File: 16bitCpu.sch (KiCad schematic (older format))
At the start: 0 parts

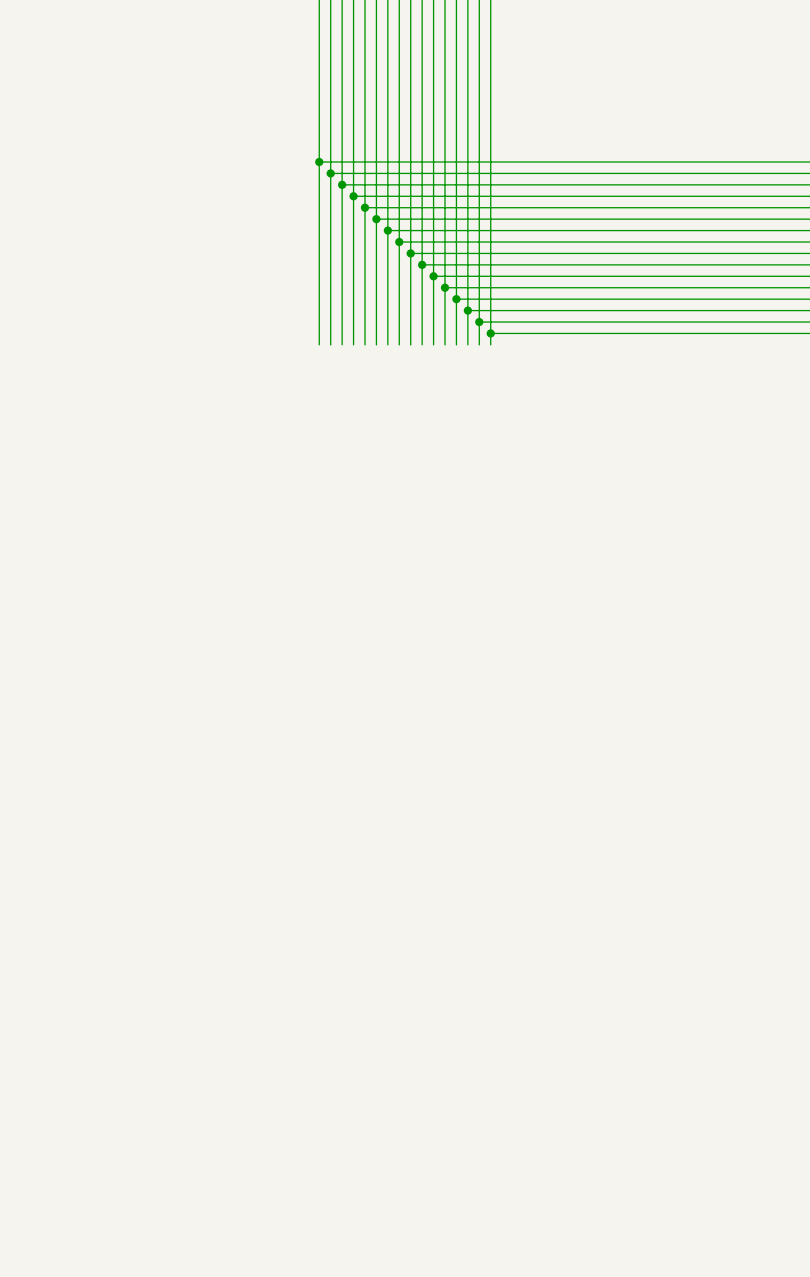
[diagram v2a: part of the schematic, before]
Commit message: Added ROM with 2 inverter cap nonsense
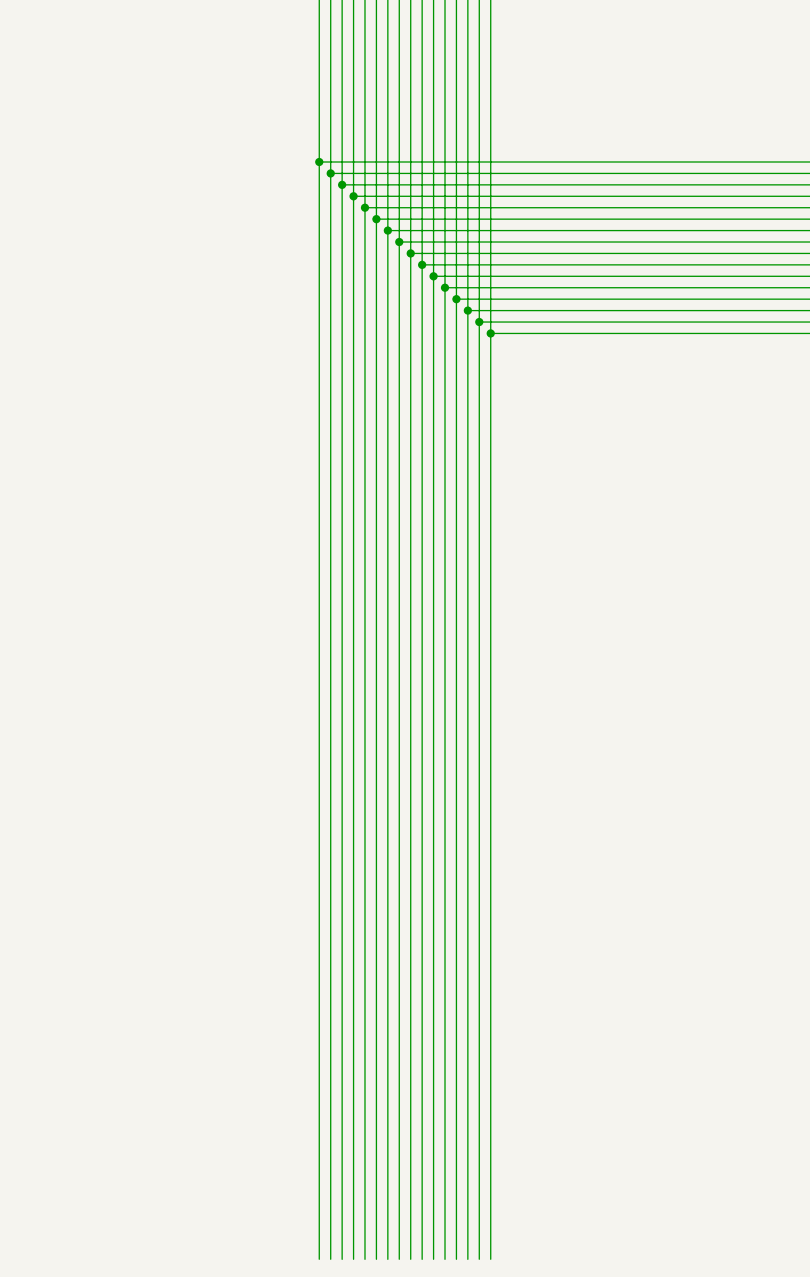
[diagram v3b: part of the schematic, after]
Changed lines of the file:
@@
 	6100 10150 6100 11200
 Connection ~ 6100 11200
-Wire Wire Line
-	6100 11200 6100 12000
 Connection ~ 6150 7300
 Connection ~ 6150 10050
 Connection ~ 6150 11250
-Wire Wire Line
-	6150 11250 6150 12000
 Connection ~ 6200 7200
 Connection ~ 6200 9950
@@
 	6200 9950 6200 10150
 Connection ~ 6200 11300
-Wire Wire Line
-	6200 11300 6200 12000
 Connection ~ 6250 7100
 Connection ~ 6250 9850
 Connection ~ 6250 11350
-Wire Wire Line
-	6250 11350 6250 12000
 Connection ~ 6300 7000
 Connection ~ 6300 9750
 Connection ~ 6300 11400
-Wire Wire Line
-	6300 11400 6300 12000
 Connection ~ 6350 6900
 Connection ~ 6350 9650
 Connection ~ 6350 11450
-Wire Wire Line
-	6350 11450 6350 12000
 Connection ~ 6400 6800
 Connection ~ 6400 9550
 Connection ~ 6400 11500
-Wire Wire Line
-	6400 11500 6400 12000
 Connection ~ 6450 6700
 Connection ~ 6450 9450
 Connection ~ 6450 11550
-Wire Wire Line
-	6450 11550 6450 12000
 Connection ~ 6500 6600
 Connection ~ 6500 9350
 Connection ~ 6500 11600
-Wire Wire Line
-	6500 11600 6500 12000
 Connection ~ 6550 6500
 Connection ~ 6550 9250
 Connection ~ 6550 11650
-Wire Wire Line
-	6550 11650 6550 12000
 Connection ~ 6600 6400
 Connection ~ 6600 9150
 Connection ~ 6600 11700
-Wire Wire Line
-	6600 11700 6600 12000
 Connection ~ 6650 6300
 Connection ~ 6650 9050
 Connection ~ 6650 11750
-Wire Wire Line
-	6650 11750 6650 12000
 Connection ~ 6700 6200
 Connection ~ 6700 8950
 Connection ~ 6700 11800
-Wire Wire Line
-	6700 11800 6700 12000
 Connection ~ 6750 6100
 Connection ~ 6750 8850
 Connection ~ 6750 11850
-Wire Wire Line
-	6750 11850 6750 12000
 Connection ~ 6800 6000
 Connection ~ 6800 8750
 Connection ~ 6800 11900
-Wire Wire Line
-	6800 11900 6800 12000
 Connection ~ 6850 5900
 Connection ~ 6850 8650
 Connection ~ 6850 11950
 Wire Wire Line
-	6850 11950 6850 12000
-Wire Wire Line
 	6200 10150 6100 10150
 Wire Wire Line
@@
 Wire Wire Line
 	6950 1950 8150 1950
+Wire Wire Line
+	6850 11950 6850 16000
+Wire Wire Line
+	6800 11900 6800 16000
+Wire Wire Line
+	6750 11850 6750 16000
+Wire Wire Line
+	6700 11800 6700 16000
+Wire Wire Line
+	6650 11750 6650 16000
+Wire Wire Line
+	6600 11700 6600 16000
+Wire Wire Line
+	6550 11650 6550 16000
+Wire Wire Line
+	6500 11600 6500 16000
+Wire Wire Line
+	6450 11550 6450 16000
+Wire Wire Line
+	6400 11500 6400 16000
+Wire Wire Line
+	6350 11450 6350 16000
+Wire Wire Line
+	6300 11400 6300 16000
+Wire Wire Line
+	6250 11350 6250 16000
+Wire Wire Line
+	6200 11300 6200 16000
+Wire Wire Line
+	6150 11250 6150 16000
+Wire Wire Line
+	6100 11200 6100 16000
 $EndSCHEMATC

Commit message: Added IR,Cu started
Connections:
- wire segments 285 -> 376

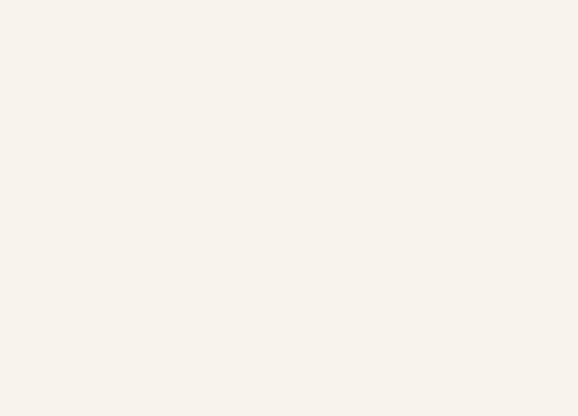
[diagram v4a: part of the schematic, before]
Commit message: Fixed power for multi part comps
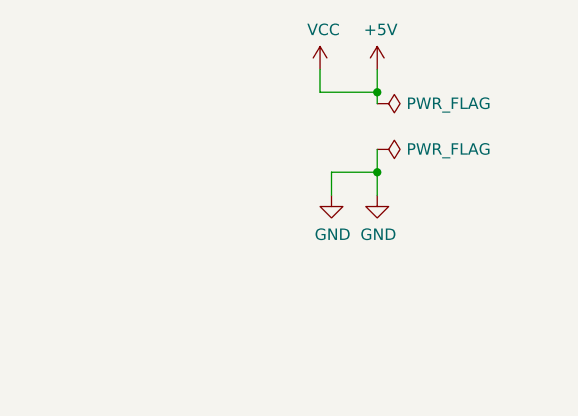
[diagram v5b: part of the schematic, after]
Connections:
- net labels added: +5V, GND, VCC
- wire segments 376 -> 384
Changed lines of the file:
@@
 	3600 7700 4050 7700
 Connection ~ 4050 7700
+$Comp
+L power:+5V #PWR03
+U 1 1 603C06D7
+P 10100 1550
+F 0 "#PWR03" H 10100 1400 50  0001 C CNN
+F 1 "+5V" H 10115 1723 50  0000 C CNN
+F 2 "" H 10100 1550 50  0001 C CNN
+F 3 "" H 10100 1550 50  0001 C CNN
+	1    10100 1550
+	1    0    0    -1
+$EndComp
+Wire Wire Line
+	10100 1550 10100 1650
+$Comp
+L power:PWR_FLAG #FLG01
+U 1 1 6041ADF9
+P 10100 1700
+F 0 "#FLG01" H 10100 1775 50  0001 C CNN
+F 1 "PWR_FLAG" V 10100 1828 50  0000 L CNN
+F 2 "" H 10100 1700 50  0001 C CNN
+F 3 "~" H 10100 1700 50  0001 C CNN
+	1    10100 1700
+	0    1    1    0
+$EndComp
+$Comp
+L power:PWR_FLAG #FLG02
+U 1 1 6041B51D
+P 10100 1900
+F 0 "#FLG02" H 10100 1975 50  0001 C CNN
+F 1 "PWR_FLAG" V 10100 2028 50  0000 L CNN
+F 2 "" H 10100 1900 50  0001 C CNN
+F 3 "~" H 10100 1900 50  0001 C CNN
+	1    10100 1900
+	0    1    1    0
+$EndComp
+$Comp
+L power:GND #PWR04
+U 1 1 6041B92E
+P 10100 2100
+F 0 "#PWR04" H 10100 1850 50  0001 C CNN
+F 1 "GND" H 10105 1927 50  0000 C CNN
+F 2 "" H 10100 2100 50  0001 C CNN
+F 3 "" H 10100 2100 50  0001 C CNN
+	1    10100 2100
+	1    0    0    -1
+$EndComp
+Wire Wire Line
+	10100 1900 10100 2000
+$Comp
+L power:GND #PWR02
+U 1 1 604BCEDD
+P 9900 2100
+F 0 "#PWR02" H 9900 1850 50  0001 C CNN
+F 1 "GND" H 9905 1927 50  0000 C CNN
+F 2 "" H 9900 2100 50  0001 C CNN
+F 3 "" H 9900 2100 50  0001 C CNN
+	1    9900 2100
+	1    0    0    -1
+$EndComp
+Wire Wire Line
+	9900 2100 9900 2000
+Wire Wire Line
+	9900 2000 10100 2000
+Connection ~ 10100 2000
+Wire Wire Line
+	10100 2000 10100 2100
+$Comp
+L power:VCC #PWR01
+U 1 1 604EB05F
+P 9850 1550
+F 0 "#PWR01" H 9850 1400 50  0001 C CNN
+F 1 "VCC" H 9865 1723 50  0000 C CNN
+F 2 "" H 9850 1550 50  0001 C CNN
+F 3 "" H 9850 1550 50  0001 C CNN
+	1    9850 1550
+	1    0    0    -1
+$EndComp
+Wire Wire Line
+	9850 1550 9850 1650
+Wire Wire Line
+	9850 1650 10100 1650
+Connection ~ 10100 1650
+Wire Wire Line
+	10100 1650 10100 1700
 $EndSCHEMATC

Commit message: Various Fixes
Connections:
- wire segments 384 -> 387

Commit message: made the CU , need to change the IR
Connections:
- wire segments 387 -> 411
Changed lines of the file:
@@
 F16 "A14" I L 8050 6950 50
 F17 "A15" I L 8050 7050 50
-F18 "SU" I R 8900 6200 50
+F18 "SU" I R 8900 6700 50
 F19 "B15" I L 8050 8850 50
 F20 "B14" I L 8050 8750 50
@@
 F33 "B1" I L 8050 7450 50
 F34 "B0" I L 8050 7350 50
-F35 "~EO" I R 8900 6300 50
+F35 "~EO" I R 8900 6600 50
 F36 "BUS0" T R 8900 7350 50
 F37 "BUS1" T R 8900 7450 50
@@
 F50 "BUS14" T R 8900 8750 50
 F51 "BUS15" T R 8900 8850 50
-F52 "~FI" I R 8900 6100 50
+F52 "~FI" I R 8900 6500 50
 F53 "CLK" I R 8900 6000 50
 F54 "CLR" I R 8900 5900 50
@@
 	7100 9400 7800 9400
 Wire Wire Line
-	7800 9400 7800 8450
-Wire Wire Line
 	7800 8450 8050 8450
 Wire Wire Line
@@
 Wire Wire Line
 	7250 7350 8050 7350
-Wire Wire Line
-	7300 7450 8050 7450
 Wire Wire Line
 	7350 7550 8050 7550
@@
 Wire Wire Line
 	7400 2100 7400 1600
-Wire Wire Line
-	6050 11550 6050 12050
-Wire Wire Line
-	6000 11500 6000 12150
-Wire Wire Line
-	5950 11450 5950 12250
-Wire Wire Line
-	5900 11400 5900 12350
-Wire Wire Line
-	5750 11250 5750 12650
-Wire Wire Line
-	5700 11200 5700 12750
-Wire Wire Line
-	5650 11150 5650 12850
-Wire Wire Line
-	5600 11100 5600 12950
-Wire Wire Line
-	5550 11050 5550 13050
-Wire Wire Line
-	5500 11000 5500 13150
-Wire Wire Line
-	5450 10950 5450 13250
-Wire Wire Line
-	5400 10900 5400 13350
 Wire Wire Line
 	5000 7250 6100 7250
@@
 	3300 3950 4400 3950
 Wire Wire Line
-	6100 11600 6100 11950
-Wire Wire Line
-	5350 10850 5350 13450
-Wire Wire Line
 	5350 9800 6400 9800
 Wire Wire Line
 	5450 9600 5450 10950
-Wire Wire Line
-	5150 11950 6100 11950
-Connection ~ 6100 11950
-Wire Wire Line
-	6100 11950 6100 15650
-Wire Wire Line
-	5150 12050 6050 12050
-Connection ~ 6050 12050
-Wire Wire Line
-	6050 12050 6050 15650
-Wire Wire Line
-	5150 12150 6000 12150
-Connection ~ 6000 12150
-Wire Wire Line
-	6000 12150 6000 15650
-Wire Wire Line
-	5150 12250 5950 12250
-Connection ~ 5950 12250
-Wire Wire Line
-	5950 12250 5950 15650
-Wire Wire Line
-	5150 12350 5900 12350
-Connection ~ 5900 12350
-Wire Wire Line
-	5900 12350 5900 15650
-Wire Wire Line
-	5150 12450 5850 12450
-Wire Wire Line
-	5850 11350 5850 12450
-Connection ~ 5850 12450
-Wire Wire Line
-	5850 12450 5850 15650
-Wire Wire Line
-	5150 12550 5800 12550
-Wire Wire Line
-	5800 11300 5800 12550
-Connection ~ 5800 12550
-Wire Wire Line
-	5800 12550 5800 15650
-Wire Wire Line
-	5150 12650 5750 12650
-Connection ~ 5750 12650
-Wire Wire Line
-	5750 12650 5750 15650
-Wire Wire Line
-	5150 12750 5700 12750
-Connection ~ 5700 12750
-Wire Wire Line
-	5700 12750 5700 15650
-Wire Wire Line
-	5150 12850 5650 12850
-Connection ~ 5650 12850
-Wire Wire Line
-	5650 12850 5650 15650
-Wire Wire Line
-	5150 12950 5600 12950
-Connection ~ 5600 12950
-Wire Wire Line
-	5600 12950 5600 15650
-Wire Wire Line
-	5150 13050 5550 13050
-Connection ~ 5550 13050
-Wire Wire Line
-	5550 13050 5550 15650
-Wire Wire Line
-	5150 13150 5500 13150
-Connection ~ 5500 13150
-Wire Wire Line
-	5500 13150 5500 15650
-Wire Wire Line
-	5150 13250 5450 13250
-Connection ~ 5450 13250
-Wire Wire Line
-	5450 13250 5450 15650
-Wire Wire Line
-	5150 13350 5400 13350
-Connection ~ 5400 13350
-Wire Wire Line
-	5400 13350 5400 15650
-Wire Wire Line
-	5150 13450 5350 13450
-Connection ~ 5350 13450
-Wire Wire Line
-	5350 13450 5350 15650
-$Sheet
-S 4350 11300 800  2400
-U 5FD099BF
-F0 "Control Unit" 50
-F1 "Control Unit.sch" 50
-F2 "Bus1" T R 5150 12050 50
-F3 "Bus0" T R 5150 11950 50
-F4 "Bus2" T R 5150 12150 50
-F5 "Bus3" T R 5150 12250 50
-F6 "Bus4" T R 5150 12350 50
-F7 "Bus5" T R 5150 12450 50
-F8 "Bus6" T R 5150 12550 50
-F9 "Bus7" T R 5150 12650 50
-F10 "Bus9" T R 5150 12850 50
-F11 "Bus10" T R 5150 12950 50
-F12 "Bus11" T R 5150 13050 50
-F13 "Bus12" T R 5150 13150 50
-F14 "Bus13" T R 5150 13250 50
-F15 "Bus14" T R 5150 13350 50
-F16 "Bus15" T R 5150 13450 50
-F17 "Bus8" T R 5150 12750 50
-F18 "I1" I L 4350 11800 50
-F19 "I0" I L 4350 11700 50
-F20 "I2" I L 4350 11900 50
-F21 "I3" I L 4350 12000 50
-F22 "I4" I L 4350 12100 50
-F23 "I5" I L 4350 12200 50
-F24 "I6" I L 4350 12300 50
-F25 "I7" I L 4350 12400 50
-F26 "CLK" I L 4350 12600 50
-$EndSheet
 Wire Wire Line
 	3100 8100 3100 11700
@@
 Wire Wire Line
 	9300 6000 8900 6000
+$Sheet
+S 4350 11300 800  2950
+U 5FD099BF
+F0 "Control Unit" 50
+F1 "Control Unit.sch" 50
+F2 "I1" I L 4350 11800 50
+F3 "I0" I L 4350 11700 50
+F4 "I2" I L 4350 11900 50
+F5 "I3" I L 4350 12000 50
+F6 "I4" I L 4350 12100 50
+F7 "I5" I L 4350 12200 50
+F8 "I6" I L 4350 12300 50
+F9 "I7" I L 4350 12400 50
+F10 "CLK" I L 4350 12600 50
+F11 "ZF" I R 5150 13150 50
+F12 "CF" I R 5150 13250 50
+F13 "~ALU_FI" O R 5150 12250 50
+F14 "ALU_SU" O R 5150 12350 50
+F15 "~ALU_EO" O R 5150 12450 50
+F16 "~R1_AI" O R 5150 12650 50
+F17 "~R1_AO" O R 5150 12750 50
+F18 "~R2_AI" O R 5150 12900 50
+F19 "~R2_AO" O R 5150 13000 50
+F20 "~RAM_AI" O L 4350 13000 50
+F21 "~RAM_AO" O L 4350 13100 50
+F22 "~RAM_MEMOE" O L 4350 13200 50
+F23 "~RAM_MEMWE" O L 4350 13300 50
+F24 "~IR_AI" O L 4350 13600 50
+F25 "~IR_AO" O L 4350 13700 50
+F26 "~IR_13AO" O L 4350 13800 50
+F27 "~PC_J" O R 5150 13500 50
+F28 "PC_CE" O R 5150 13600 50
+F29 "~PC_CO" O R 5150 13700 50
+F30 "CLR" O R 5150 13850 50
+F31 "~CLR" O R 5150 14000 50
+$EndSheet
+Wire Wire Line
+	6100 11600 6100 15650
+Wire Wire Line
+	6050 11550 6050 15650
+Wire Wire Line
+	6000 11500 6000 15650
+Wire Wire Line
+	5950 11450 5950 15650
+Wire Wire Line
+	5900 11400 5900 15650
+Wire Wire Line
+	5850 11350 5850 15650
+Wire Wire Line
+	5800 11300 5800 15650
+Wire Wire Line
+	5750 11250 5750 15650
+Wire Wire Line
+	5700 11200 5700 15650
+Wire Wire Line
+	5650 11150 5650 15650
+Wire Wire Line
+	5600 11100 5600 15650
+Wire Wire Line
+	5550 11050 5550 15650
+Wire Wire Line
+	5500 11000 5500 15650
+Wire Wire Line
+	5450 10950 5450 15650
+Wire Wire Line
+	5400 10900 5400 15650
+Wire Wire Line
+	5350 10850 5350 15650
+Wire Wire Line
+	8900 5450 10550 5450
+Wire Wire Line
+	10550 5450 10550 13150
+Wire Wire Line
+	10550 13150 5150 13150
+Wire Wire Line
+	8900 5550 10500 5550
+Wire Wire Line
+	10500 5550 10500 13250
+Wire Wire Line
+	10500 13250 5150 13250
+Wire Wire Line
+	5150 12250 10450 12250
+Wire Wire Line
+	10450 12250 10450 6500
+Wire Wire Line
+	10450 6500 8900 6500
+Wire Wire Line
+	5150 12350 10400 12350
+Wire Wire Line
+	10400 12350 10400 6700
+Wire Wire Line
+	10400 6700 8900 6700
+Wire Wire Line
+	5150 12450 10350 12450
+Wire Wire Line
+	10350 12450 10350 6600
+Wire Wire Line
+	10350 6600 8900 6600
+Wire Wire Line
+	7300 7450 8050 7450
+Wire Wire Line
+	7100 7450 7150 7450
+Wire Wire Line
+	7150 7450 7150 7250
+Wire Wire Line
+	7150 7250 8500 7250
+Wire Wire Line
+	8500 7250 8500 12650
+Wire Wire Line
+	8500 12650 5150 12650
+Wire Wire Line
+	5150 12750 7150 12750
+Wire Wire Line
+	7150 12750 7150 7550
+Wire Wire Line
+	7150 7550 7100 7550
+Wire Wire Line
+	7800 9400 7800 8450
+Wire Wire Line
+	5150 12900 10300 12900
+Wire Wire Line
+	10300 12900 10300 4700
+Wire Wire Line
+	10300 4700 7100 4700
+Wire Wire Line
+	5150 13000 10200 13000
+Wire Wire Line
+	10200 13000 10200 4800
+Wire Wire Line
+	10200 4800 7100 4800
+Wire Wire Line
+	5150 13500 10600 13500
+Wire Wire Line
+	10600 13500 10600 2350
+Wire Wire Line
+	10600 2350 7200 2350
+Wire Wire Line
+	5150 13600 10650 13600
+Wire Wire Line
+	10650 13600 10650 2450
+Wire Wire Line
+	10650 2450 7200 2450
+Wire Wire Line
+	5150 13700 10700 13700
+Wire Wire Line
+	10700 13700 10700 2550
+Wire Wire Line
+	10700 2550 7200 2550
+Wire Wire Line
+	4350 13000 2000 13000
+Wire Wire Line
+	2000 13000 2000 4600
+Wire Wire Line
+	2000 4600 4400 4600
+Wire Wire Line
+	4350 13100 1950 13100
+Wire Wire Line
+	1950 13100 1950 4500
+Wire Wire Line
+	1950 4500 4400 4500
+Wire Wire Line
+	4350 13200 1850 13200
+Wire Wire Line
+	1850 13200 1850 4750
+Wire Wire Line
+	1850 4750 4400 4750
+Wire Wire Line
+	4350 13300 1800 13300
+Wire Wire Line
+	1800 13300 1800 4850
+Wire Wire Line
+	1800 4850 4400 4850
+Wire Wire Line
+	4350 13600 2750 13600
+Wire Wire Line
+	2750 13600 2750 7550
+Wire Wire Line
+	2750 7550 4350 7550
+Wire Wire Line
+	2650 7450 4350 7450
+Wire Wire Line
+	4350 13800 2650 13800
+Wire Wire Line
+	2650 7450 2650 13800
 $EndSCHEMATC
